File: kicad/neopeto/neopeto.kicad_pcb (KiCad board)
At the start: 2 copper layers, 99.1 x 74.9 mm, 147 parts, among them J1 Conn_01x10_Pin, J2 Conn_01x10_Pin, J3 Conn_01x10_Pin, J4 PJ-307, U1 74HC00, U10 74HC590, U11 74HC590, U12 74HC590, U13 74HC245, U14 K6X4008C1F, U15 74HC245, U16 74HC245, U17 LM358LV, U18 LM358LV, U19 LM358LV, U2 74LVC1G00, U21 TLC7258C, U22 TLC7258C, U23 74HC4017, U24 74HC86, U25 74AUP1G08, U26 74LVC1G332, U27 74LVC1G332, U3 CH32V003JxMx, U4 82C55A_PLCC, U5 82C54_PLCC, U6 74HC139, U7 74HC245, U8 74HC245, U9 74HC245, X1 ECS-2520MV-12MHZ

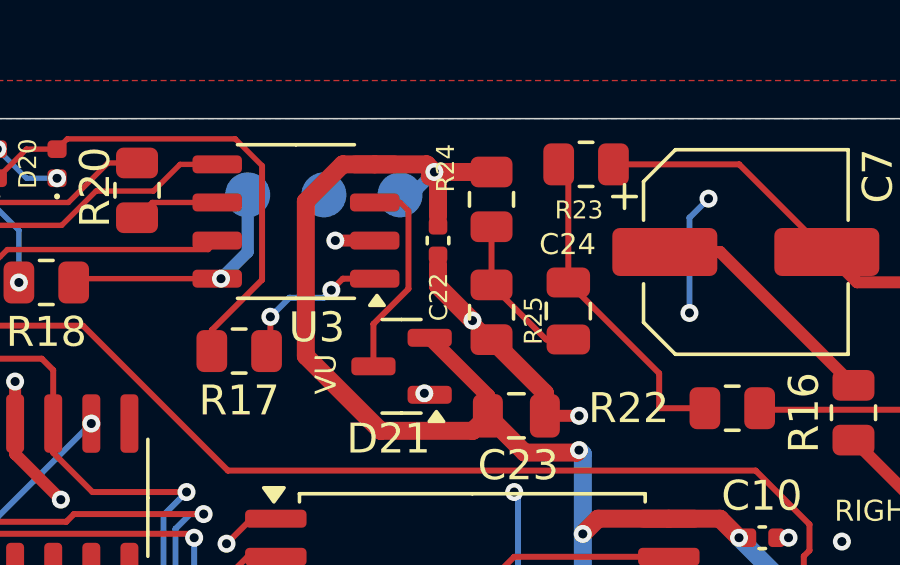
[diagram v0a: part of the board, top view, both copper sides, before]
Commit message: fixed missing connection to VU on ch32v003
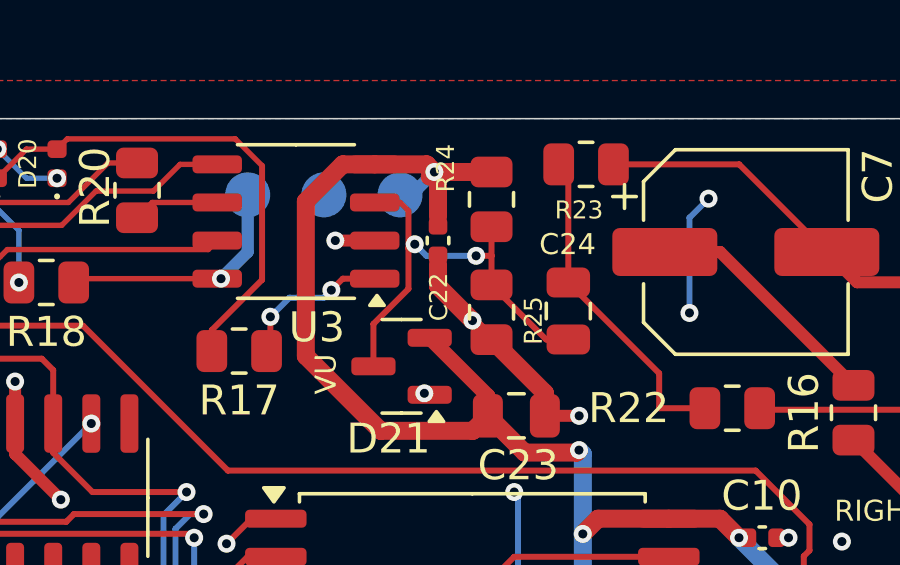
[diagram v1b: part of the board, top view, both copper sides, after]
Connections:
- C24 pad 1: Net-(C24-Pad1) -> /VU
- R24 pad 1: Net-(C24-Pad1) -> /VU
- R25 pad 2: Net-(C24-Pad1) -> /VU
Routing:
- net /VU: track 6.91 -> 15.1 mm, vias 0 -> 2
- net Net-(C24-Pad1): track 5.25 -> 0.00 mm

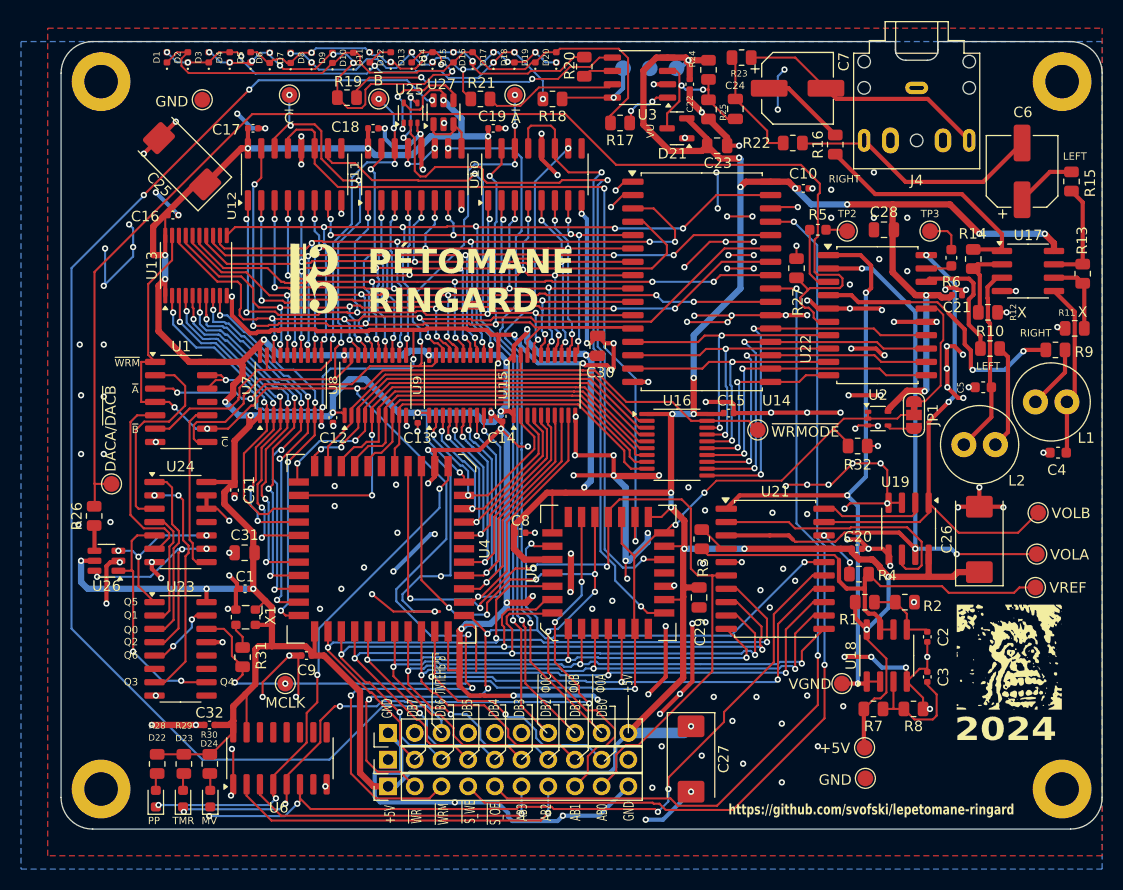
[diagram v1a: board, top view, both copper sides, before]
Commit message: update led resistor values
470*2 / 20 makes for a rather dim display
the leds are specified for 25mA at 1.6V

100 ohm * 2 -> 17mA, bright enough not to look good next to other leds
on my desk and on the same board
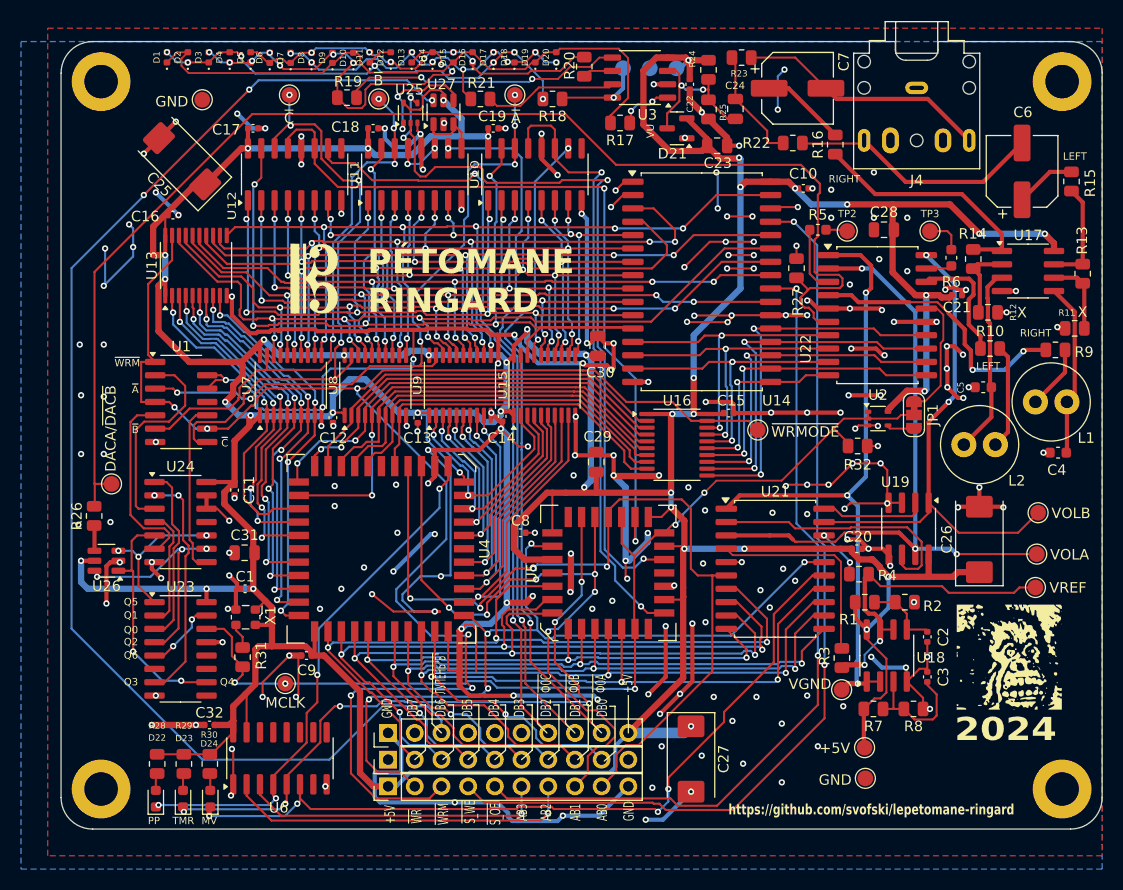
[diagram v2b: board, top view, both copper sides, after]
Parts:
- moved R3 17.5 mm to (135.3, 84.1)
- moved C29 16.2 mm to (111.9, 65.4), turned to -90 degrees
- moved TP6 0.58 mm to (135.2, 87.1)
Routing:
- net Net-(U21-REFA): track 3.09 -> 20.1 mm
- net /VREF: track 43.3 -> 31.3 mm, vias 0 -> 2
- net GND: track 544.4 -> 538.0 mm, vias 217 -> 216
- net /~{CS_MVOL}: track 76.6 -> 77.5 mm
